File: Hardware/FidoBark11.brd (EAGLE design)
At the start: 40.3 x 45.7 mm, 25 parts, among them T1 BPX81, U1 MB85RC256VPF-G-JNERE2, U2 ADMP401

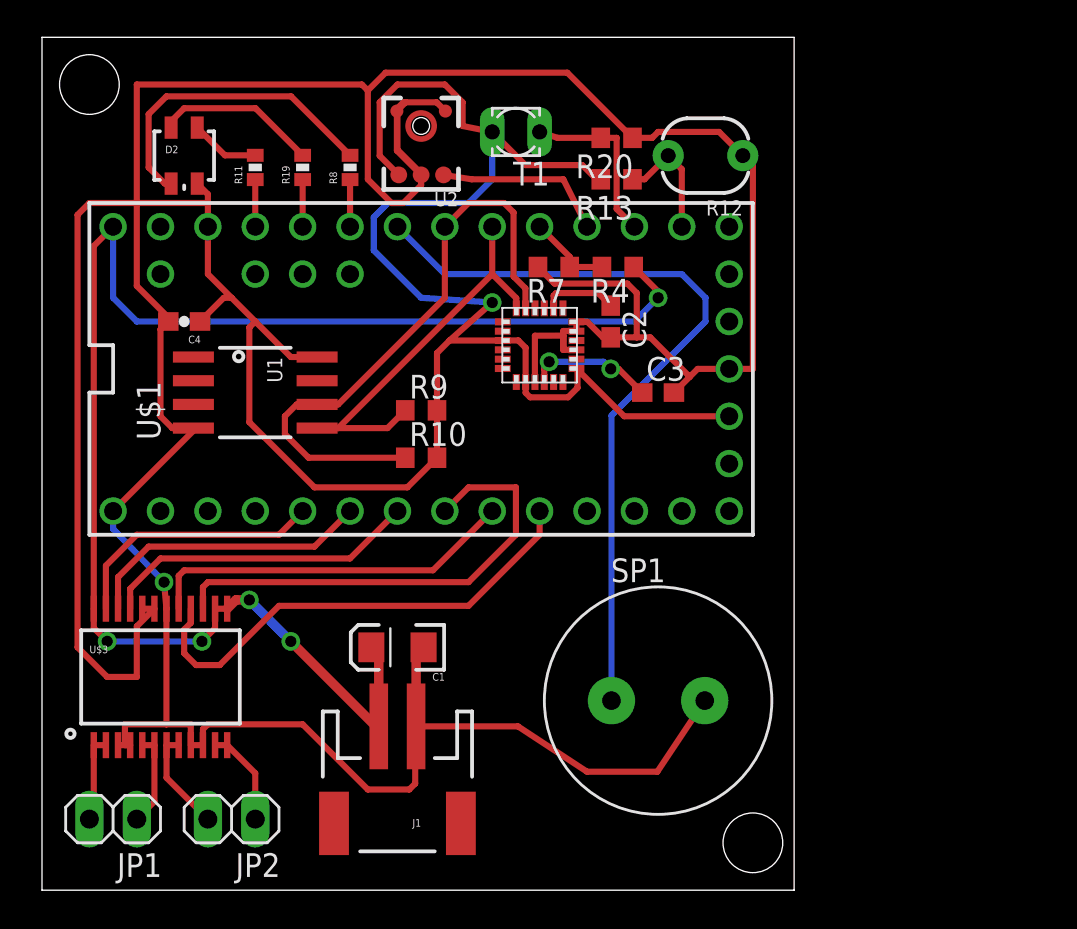
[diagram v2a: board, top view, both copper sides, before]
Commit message: added esp8266
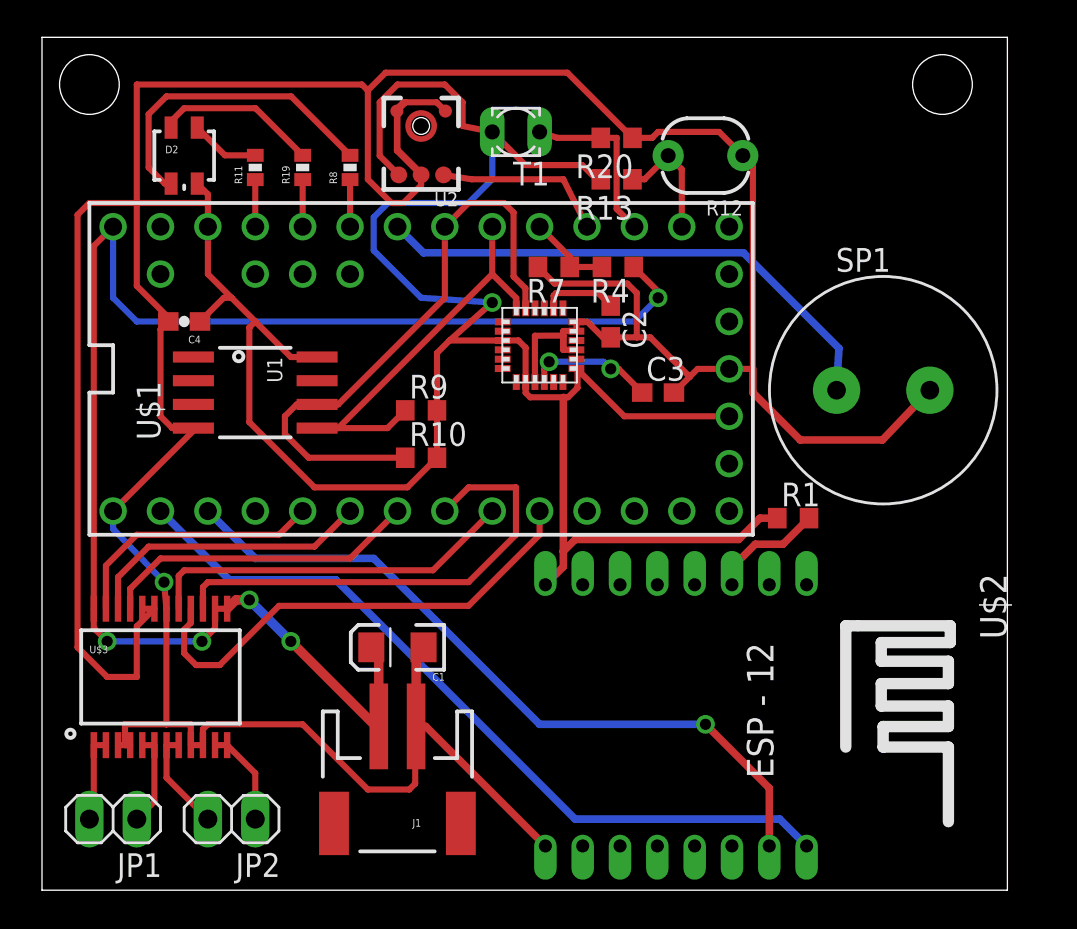
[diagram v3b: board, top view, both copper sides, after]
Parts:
- added R1: 10k, rcl:R0603
- added U$2: ESP12, esp8266modules:ESP12
- moved SP1 20.6 mm to (45.1, 26.8)
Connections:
- new net N$2: R1.2, U$2.CH_PD
- new net RX: U$1.0, U$2.TX
- new net TX: U$1.1, U$2.RX
- net 3.3V: now also R1.1, U$2.VCC
- net GND: now also U$2.GND
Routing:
- net RX: track 0.00 -> 42.1 mm
- net TX: track 0.00 -> 39.3 mm, vias 0 -> 1
- net 3.3V: track 139.6 -> 162.2 mm
- net PIEZO: track 41.8 -> 28.6 mm
- net N$2: track 0.00 -> 6.15 mm
- net GND: track 181.9 -> 186.2 mm
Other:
- board size 40.3 x 45.7 mm -> 51.7 x 45.7 mm
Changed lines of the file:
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@@
 <board>
 <plain>
-<wire x1="0" y1="0" x2="40.31" y2="0" width="0" layer="20"/>
-<wire x1="40.31" y1="0" x2="40.31" y2="45.71" width="0" layer="20"/>
-<wire x1="40.31" y1="45.71" x2="0" y2="45.71" width="0" layer="20"/>
+<wire x1="0" y1="0" x2="51.74" y2="0" width="0" layer="20"/>
+<wire x1="51.74" y1="0" x2="51.74" y2="45.71" width="0" layer="20"/>
+<wire x1="51.74" y1="45.71" x2="0" y2="45.71" width="0" layer="20"/>
 <wire x1="0" y1="45.71" x2="0" y2="0" width="0" layer="20"/>
 <hole x="2.54" y="43.18" drill="3.2"/>
-<hole x="38.1" y="2.54" drill="3.2"/>
+<hole x="48.26" y="43.18" drill="3.2"/>
 </plain>
 <attributes>
@@
 <element name="R8" library="SparkFun" package="0402-RES" value="200" x="16.51" y="38.735" rot="R90"/>
 <element name="R9" library="rcl" package="R0603" value="10k" x="20.32" y="25.7175"/>
-<element name="SP1" library="adafruit" package="PS12" value="SPEAKER/PS12" x="33.02" y="10.16"/>
+<element name="SP1" library="adafruit" package="PS12" value="SPEAKER/PS12" x="45.085" y="26.797"/>
 <element name="T1" library="opto-trans-siemens" package="BPX81" value="BPX81" x="25.4" y="40.64" rot="R180">
 <attribute name="OC_NEWARK" value="unknown" x="25.4" y="40.64" size="1.778" layer="27" rot="R180" display="off"/>
@@
 <element name="U1" library="microbuilder" package="SOIC8_208MIL" value="MB85RC256VPF-G-JNERE2" x="11.43" y="26.67" rot="R270"/>
 <element name="U2" library="SparkFun" package="ADMP401" value="ADMP401" x="20.32" y="40.9575" rot="R180"/>
+<element name="U$2" library="esp8266modules" package="ESP12" value="ESP12" x="35.179" y="9.271" rot="R270"/>
+<element name="R1" library="rcl" package="R0603" value="10k" x="40.259" y="19.939"/>
 </elements>
 <signals>
@@
 <wire x1="25.92" y1="27.235" x2="25.92" y2="26.658" width="0.3302" layer="1"/>
 <wire x1="25.92" y1="26.658" x2="26.162" y2="26.416" width="0.3302" layer="1"/>
-<wire x1="26.162" y1="26.416" x2="28.194" y2="26.416" width="0.3302" layer="1"/>
+<wire x1="26.162" y1="26.416" x2="27.94" y2="26.416" width="0.3302" layer="1"/>
+<wire x1="27.94" y1="26.416" x2="28.194" y2="26.416" width="0.3302" layer="1"/>
 <wire x1="28.194" y1="26.416" x2="28.702" y2="26.924" width="0.3302" layer="1"/>
 <wire x1="28.702" y1="26.924" x2="28.702" y2="27.903" width="0.3302" layer="1"/>
@@
 <wire x1="22.86" y1="36.83" x2="24.13" y2="38.1" width="0.3302" layer="16"/>
 <wire x1="24.13" y1="38.1" x2="24.13" y2="40.64" width="0.3302" layer="16"/>
+<contactref element="U$2" pad="VCC"/>
+<contactref element="R1" pad="1"/>
+<wire x1="39.409" y1="19.939" x2="38.481" y2="19.939" width="0.4064" layer="1"/>
+<wire x1="38.481" y1="19.939" x2="37.338" y2="18.796" width="0.4064" layer="1"/>
+<wire x1="37.338" y1="18.796" x2="28.575" y2="18.796" width="0.4064" layer="1"/>
+<wire x1="28.575" y1="18.796" x2="27.94" y2="18.161" width="0.4064" layer="1"/>
+<wire x1="27.94" y1="18.161" x2="27.94" y2="17.332" width="0.4064" layer="1"/>
+<wire x1="26.979" y1="16.371" x2="27.94" y2="17.332" width="0.4064" layer="1"/>
+<wire x1="27.94" y1="18.161" x2="27.94" y2="26.416" width="0.4064" layer="1"/>
 </signal>
 <signal name="GND">
@@
 <wire x1="20.0025" y1="5.715" x2="20.0025" y2="8.7325" width="0.3302" layer="1"/>
 <wire x1="20.0025" y1="8.7325" x2="20.05" y2="8.78" width="0.3302" layer="1"/>
-<wire x1="20.05" y1="8.78" x2="25.51" y2="8.78" width="0.3302" layer="1"/>
-<wire x1="25.51" y1="8.78" x2="29.21" y2="6.35" width="0.3302" layer="1"/>
-<wire x1="29.21" y1="6.35" x2="32.98" y2="6.35" width="0.3302" layer="1"/>
-<wire x1="32.98" y1="6.35" x2="35.52" y2="10.16" width="0.3302" layer="1"/>
 <wire x1="20.45" y1="13.0175" x2="20.05" y2="12.6175" width="0.508" layer="1"/>
 <wire x1="20.05" y1="12.6175" x2="20.05" y2="8.78" width="0.508" layer="1"/>
@@
 <wire x1="31.369" y1="32.512" x2="31.877" y2="32.004" width="0.3302" layer="1"/>
 <wire x1="31.877" y1="32.004" x2="31.877" y2="29.63" width="0.3302" layer="1"/>
+<contactref element="U$2" pad="GND"/>
+<wire x1="47.585" y1="26.797" x2="45.045" y2="24.13" width="0.4064" layer="1"/>
+<wire x1="45.045" y1="24.13" x2="40.64" y2="24.13" width="0.4064" layer="1"/>
+<wire x1="40.64" y1="24.13" x2="38.1" y2="26.67" width="0.4064" layer="1"/>
+<wire x1="38.1" y1="26.67" x2="38.1" y2="27.94" width="0.4064" layer="1"/>
+<wire x1="26.979" y1="2.371" x2="20.57" y2="8.78" width="0.4064" layer="1"/>
+<wire x1="20.57" y1="8.78" x2="20.05" y2="8.78" width="0.4064" layer="1"/>
 </signal>
 <signal name="N$1">
@@
 <contactref element="SP1" pad="P$1"/>
 <contactref element="U$1" pad="20/A6"/>
-<wire x1="30.52" y1="10.16" x2="30.52" y2="25.44" width="0.3302" layer="16"/>
-<wire x1="30.52" y1="25.44" x2="35.56" y2="30.48" width="0.3302" layer="16"/>
-<wire x1="35.56" y1="30.48" x2="35.56" y2="31.75" width="0.3302" layer="16"/>
-<wire x1="35.56" y1="31.75" x2="34.29" y2="33.02" width="0.3302" layer="16"/>
-<wire x1="34.29" y1="33.02" x2="21.59" y2="33.02" width="0.3302" layer="16"/>
-<wire x1="21.59" y1="33.02" x2="19.05" y2="35.56" width="0.3302" layer="16"/>
+<wire x1="42.585" y1="26.797" x2="42.712" y2="29.043" width="0.4064" layer="16"/>
+<wire x1="42.712" y1="29.043" x2="37.592" y2="34.163" width="0.4064" layer="16"/>
+<wire x1="37.592" y1="34.163" x2="20.447" y2="34.163" width="0.4064" layer="16"/>
+<wire x1="20.447" y1="34.163" x2="19.05" y2="35.56" width="0.4064" layer="16"/>
 </signal>
 <signal name="ADC_VIS">
@@
 <wire x1="6.92" y1="41.21" x2="6.92" y2="40.87" width="0.3302" layer="1"/>
 </signal>
+<signal name="RX">
+<contactref element="U$1" pad="0"/>
+<contactref element="U$2" pad="TX"/>
+<wire x1="6.35" y1="20.32" x2="10.033" y2="16.637" width="0.4064" layer="16"/>
+<wire x1="10.033" y1="16.637" x2="15.748" y2="16.637" width="0.4064" layer="16"/>
+<wire x1="15.748" y1="16.637" x2="28.575" y2="3.81" width="0.4064" layer="16"/>
+<wire x1="28.575" y1="3.81" x2="39.54" y2="3.81" width="0.4064" layer="16"/>
+<wire x1="39.54" y1="3.81" x2="40.979" y2="2.371" width="0.4064" layer="16"/>
+</signal>
+<signal name="TX">
+<contactref element="U$1" pad="1"/>
+<contactref element="U$2" pad="RX"/>
+<wire x1="38.979" y1="2.371" x2="38.979" y2="5.471" width="0.4064" layer="1"/>
+<wire x1="38.979" y1="5.471" x2="35.56" y2="8.89" width="0.4064" layer="1"/>
+<via x="35.56" y="8.89" extent="1-16" drill="0.6" shape="square"/>
+<wire x1="35.56" y1="8.89" x2="26.67" y2="8.89" width="0.4064" layer="16"/>
+<wire x1="26.67" y1="8.89" x2="17.78" y2="17.78" width="0.4064" layer="16"/>
+<wire x1="17.78" y1="17.78" x2="11.43" y2="17.78" width="0.4064" layer="16"/>
+<wire x1="11.43" y1="17.78" x2="8.89" y2="20.32" width="0.4064" layer="16"/>
+</signal>
+<signal name="N$2">
+<contactref element="R1" pad="2"/>
+<contactref element="U$2" pad="CH_PD"/>
+<wire x1="36.979" y1="16.371" x2="36.979" y2="17.294" width="0.4064" layer="1"/>
+<wire x1="36.979" y1="17.294" x2="38.227" y2="18.542" width="0.4064" layer="1"/>
+<wire x1="38.227" y1="18.542" x2="39.712" y2="18.542" width="0.4064" layer="1"/>
+<wire x1="39.712" y1="18.542" x2="41.109" y2="19.939" width="0.4064" layer="1"/>
+</signal>
 </signals>

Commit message: pcb review cleaning
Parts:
- U2: value ADMP401 -> SPW2430
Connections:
- new net N$6: U$4.9
- net GND: no longer U$4.9
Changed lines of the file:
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@@
 <element name="U$4" library="invensense" package="QFN.24.4X4" value="MPU-9150.QFN" x="26.67" y="29.21"/>
 <element name="U1" library="microbuilder" package="SOIC8_208MIL" value="MB85RC256VPF-G-JNERE2" x="11.43" y="26.67" rot="R270"/>
-<element name="U2" library="SparkFun" package="ADMP401" value="ADMP401" x="20.32" y="40.9575" rot="R180"/>
+<element name="U2" library="SparkFun" package="ADMP401" value="SPW2430" x="20.32" y="40.9575" rot="R180"/>
 <element name="U$2" library="esp8266modules" package="ESP12" value="ESP12" x="35.179" y="9.271" rot="R270"/>
 <element name="R1" library="rcl" package="R0603" value="10k" x="40.259" y="19.939"/>
@@
 <contactref element="U$4" pad="17"/>
 <contactref element="U$4" pad="18"/>
-<contactref element="U$4" pad="9"/>
 <contactref element="C3" pad="2"/>
 <contactref element="C2" pad="2"/>
@@
 <wire x1="27.944" y1="29.722" x2="26.416" y2="29.718" width="0.3302" layer="1"/>
 <wire x1="26.416" y1="29.718" x2="26.416" y2="27.239" width="0.3302" layer="1"/>
-<wire x1="26.416" y1="27.239" x2="26.42" y2="27.235" width="0.3302" layer="1"/>
 <wire x1="28.645" y1="30.46" x2="29.23" y2="30.46" width="0.3302" layer="1"/>
 <wire x1="29.23" y1="30.46" x2="30.06" y2="29.63" width="0.3302" layer="1"/>
@@
 <wire x1="39.712" y1="18.542" x2="41.109" y2="19.939" width="0.4064" layer="1"/>
 </signal>
+<signal name="N$6">
+<contactref element="U$4" pad="9"/>
+</signal>
 </signals>

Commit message: corrections 1
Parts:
- added C5, C6, C7: 0.1uF, resistor:C0603
- R10, R9: value 10k -> 2k
- moved R4 12.0 mm to (18.9, 32.4), turned to 90 degrees
- moved C1 7.30 mm to (12.8, 9.21), turned to 90 degrees
- moved C3 3.91 mm to (33.9, 22.9), turned to 180 degrees
- moved U$4 3.81 mm to (26.7, 25.4)
- moved C2 1.25 mm to (30.0, 29.3), turned to 315 degrees
- moved R7 1.02 mm to (27.4, 32.4), turned to 270 degrees
- turned SP1 to 270 degrees
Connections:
- net ADC_BAT renamed ADC_BTR
- removed net N$6: U$4.9
- net 3.3V: now also C5.1, C6.1, C7.1
- net GND: now also C5.2, C6.2, C7.2
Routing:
- net 3.3V: track 162.2 -> 129.5 mm, vias 1 -> 0
- net V_BATT: track 82.5 -> 63.4 mm
- net ADC_BTR: track 4.56 -> 14.8 mm
- net GND: track 186.2 -> 180.2 mm, vias 1 -> 2
- net SCL: track 32.8 -> 36.5 mm
- net N$8: track 6.84 -> 10.3 mm, vias 2 -> 0
- net SDA: track 21.7 -> 20.5 mm
- net N$9: track 4.08 -> 3.37 mm

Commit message: corrections 2
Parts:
- turned C7 to 180 degrees
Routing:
- net 3.3V: track 129.5 -> 150.4 mm
- net GND: track 180.2 -> 191.4 mm
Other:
- board size 51.7 x 45.7 mm -> 51.7 x 44.4 mm

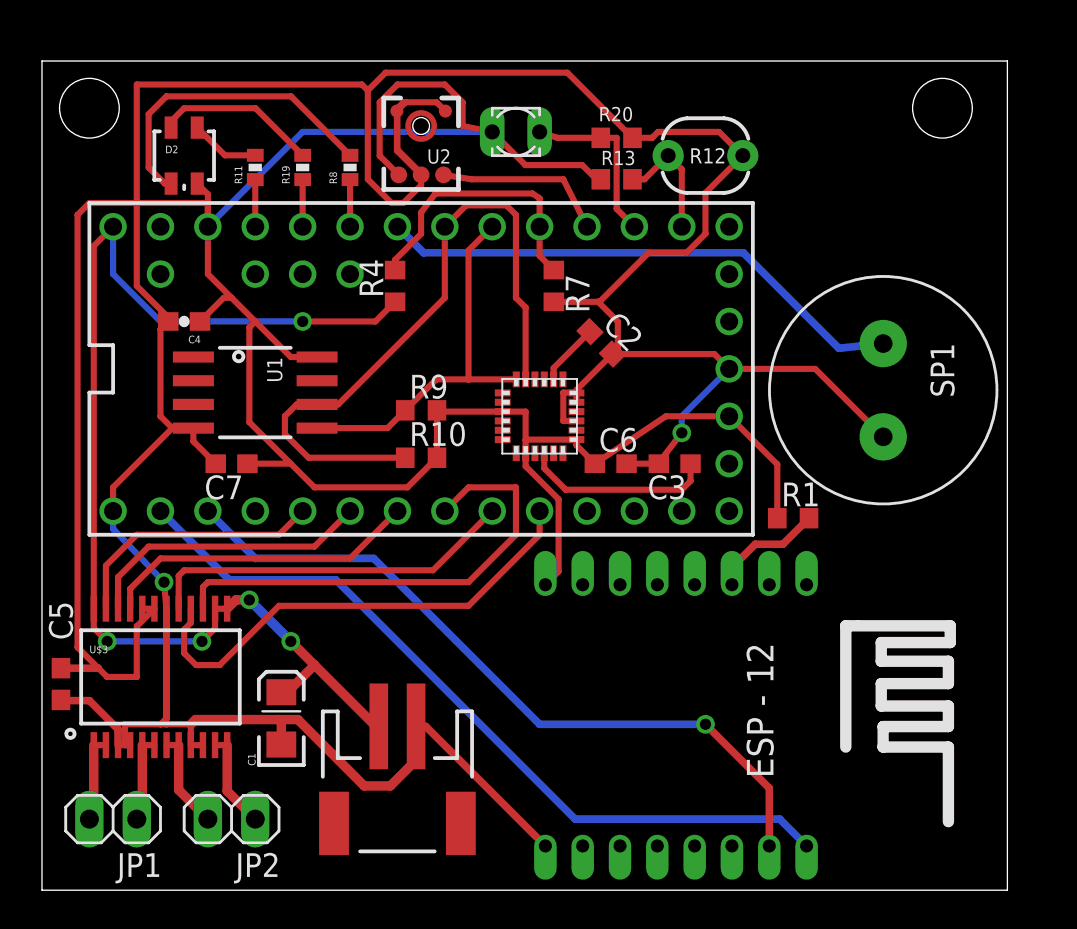
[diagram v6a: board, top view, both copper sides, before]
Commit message: manufacturing provisions
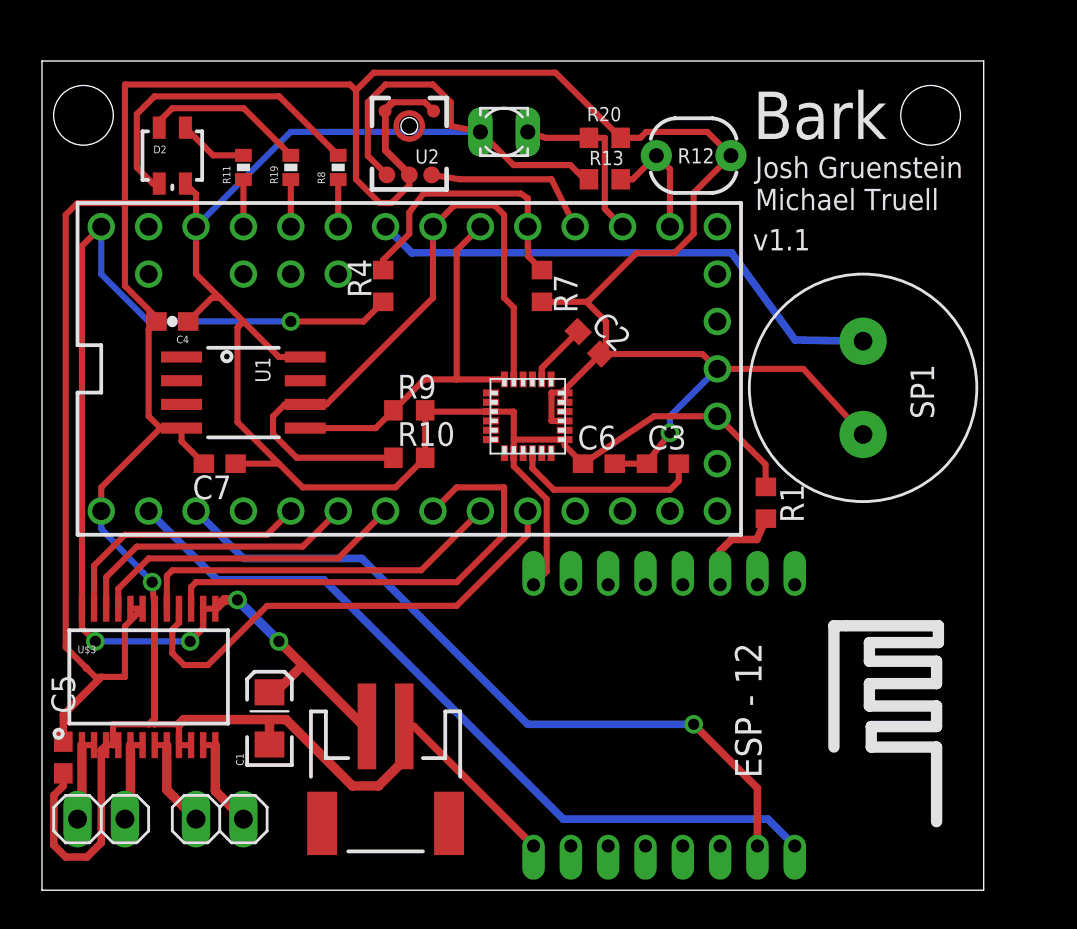
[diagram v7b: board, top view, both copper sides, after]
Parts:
- moved C5 3.94 mm to (1.14, 7.11)
- moved R1 1.68 mm to (38.8, 20.8), turned to 270 degrees
- moved SP1 1.09 mm to (44.0, 26.9)
- moved R12 0.64 mm to (34.9, 39.4)
- moved U$2 0.64 mm to (34.5, 9.27)
- moved C2 0.64 mm to (29.3, 29.3)
- moved C6 0.64 mm to (29.8, 22.9)
- moved J1 0.64 mm to (18.4, 5.08)
- moved R10 0.64 mm to (19.7, 23.2)
- moved R8 0.64 mm to (15.9, 38.7)
- moved R9 0.64 mm to (19.7, 25.7)
- moved U$1 0.64 mm to (21.0, 27.9)
- moved U$4 0.64 mm to (26.0, 25.4)
- moved U2 0.64 mm to (19.7, 41.0)
- moved JP1 0.64 mm to (3.17, 3.81)
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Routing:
- net GND: track 191.4 -> 199.0 mm
- net N$2: track 6.15 -> 5.26 mm
- net 3.3V: track 150.4 -> 149.8 mm
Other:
- board size 51.7 x 44.4 mm -> 50.5 x 44.4 mm
- board text added: "Bark"
- board text added: "Josh Gruenstein Michael Truell"
- board text added: "v1.1"
